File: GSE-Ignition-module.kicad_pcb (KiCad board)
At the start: 2 copper layers, 1 part, among them U1 Pico

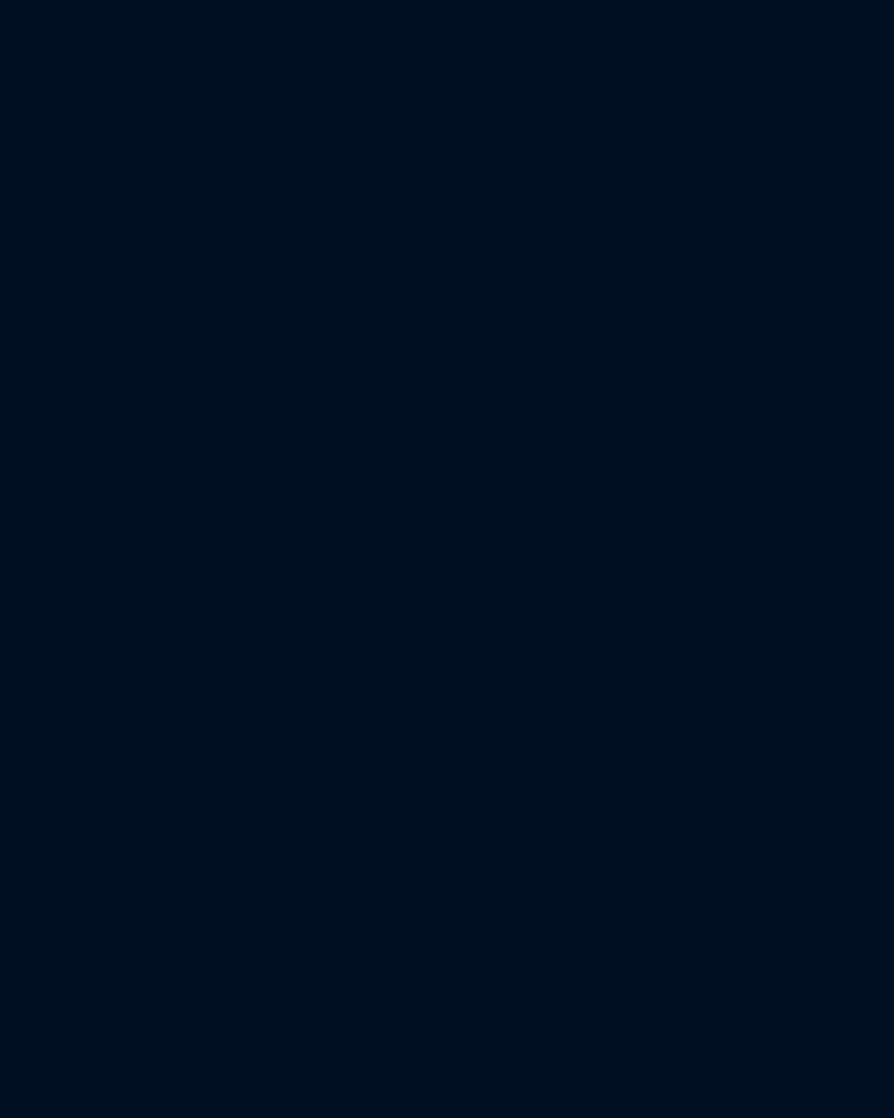
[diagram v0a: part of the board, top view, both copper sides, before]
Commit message: Add .gitignore file to ignore GSE-Ignition-module-backups and fp-info-cache
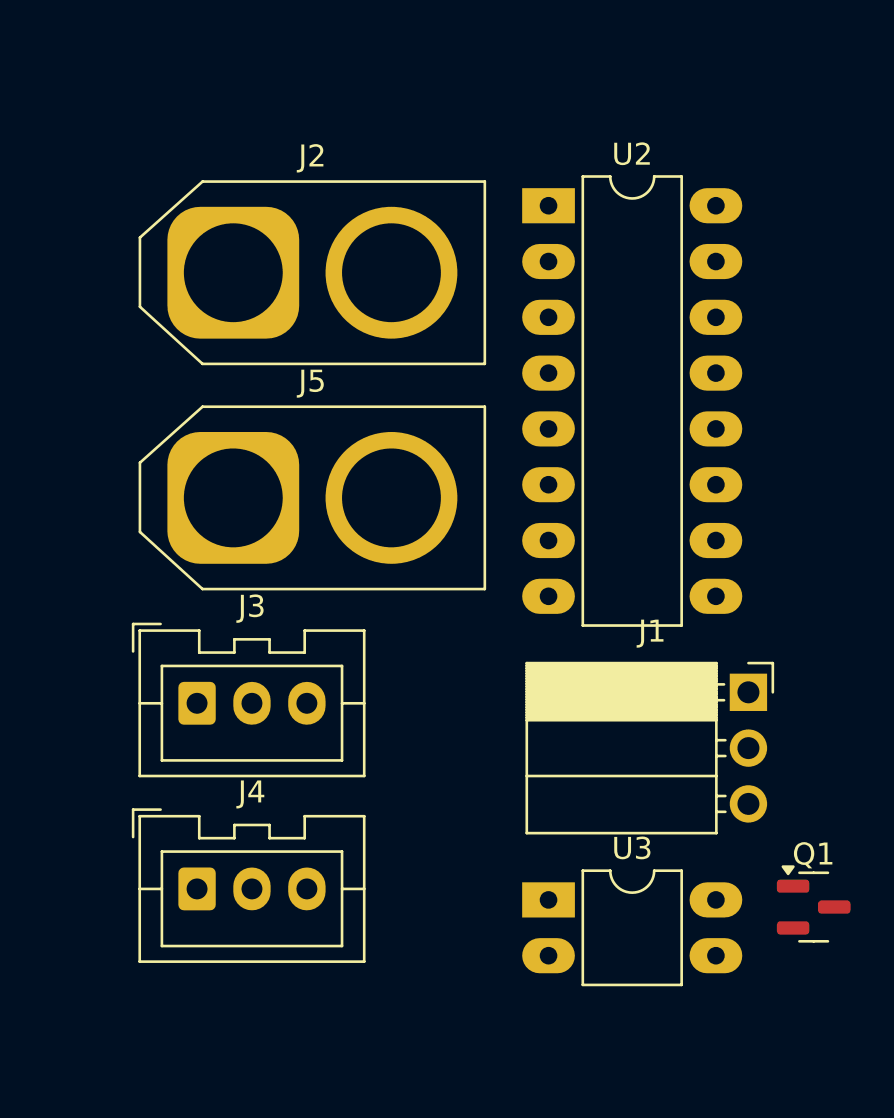
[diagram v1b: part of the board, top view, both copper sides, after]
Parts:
- added J1: DCDC-Regulator-12Vto3.3V, Connector_PinSocket_2.54mm:PinSocket_1x03_P2.54mm_Horizontal, F.Cu at (158.6, 96.2)
- added J2: Conn_01x02, Connector_AMASS:AMASS_XT60-M_1x02_P7.20mm_Vertical, F.Cu at (135.1, 77.1)
- added J3: RS232C-1, Connector_JST:JST_XA_B03B-XASK-1_1x03_P2.50mm_Vertical, F.Cu at (133.5, 96.7)
- added J4: RS232C-2, Connector_JST:JST_XA_B03B-XASK-1_1x03_P2.50mm_Vertical, F.Cu at (133.5, 105.2)
- added J5: Igniter-1, Connector_AMASS:AMASS_XT60-F_1x02_P7.20mm_Vertical, F.Cu at (135.1, 87.4)
- added Q1: BSS138, Package_TO_SOT_SMD:SOT-23, F.Cu at (161.6, 106.0)
- added U2: ADM3202ANZ, Package_DIP:DIP-16_W7.62mm_LongPads, F.Cu at (149.5, 74.1)
- added U3: TLP241A, Package_DIP:DIP-4_W7.62mm_LongPads, F.Cu at (149.5, 105.7)
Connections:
- U1 pad 1: unconnected-(U1-GPIO0-Pad1) -> RS232C-TX1-IN
- U1 pad 14: unconnected-(U1-GPIO10-Pad14) -> /Igniter-signal
- U1 pad 2: unconnected-(U1-GPIO1-Pad2) -> RS232C-RX1-OUT
- U1 pad 3: unconnected-(U1-GND-Pad3) -> GND
- U1 pad 38: unconnected-(U1-GND-Pad38) -> GND
- U1 pad 39: unconnected-(U1-VSYS-Pad39) -> +3.3V
